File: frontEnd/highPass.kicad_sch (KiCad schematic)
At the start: 15 parts, among them U101 BGS12P2L6E6327XTSA1, U102 BGS12P2L6E6327XTSA1

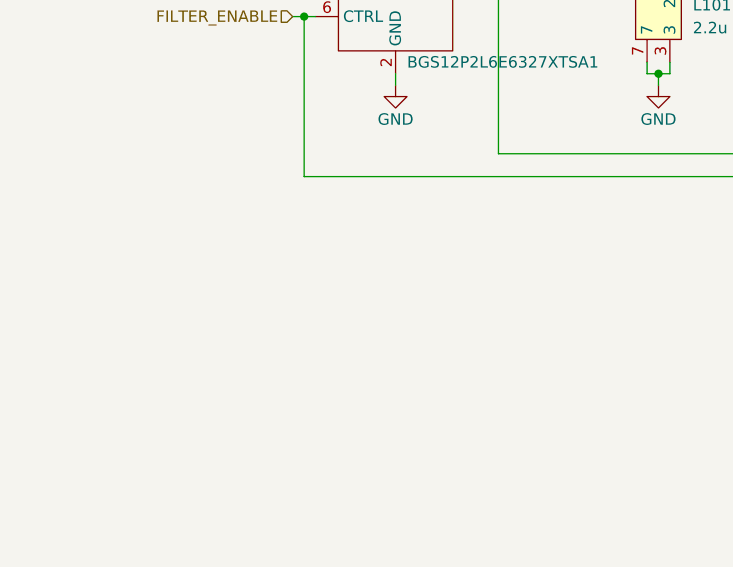
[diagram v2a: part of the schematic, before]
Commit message: add leds for each filter block
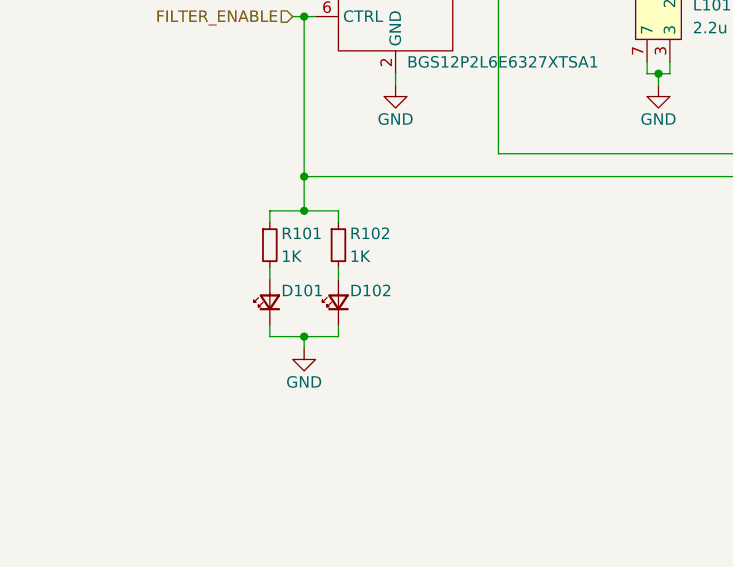
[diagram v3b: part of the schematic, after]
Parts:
- added D101, D102: LED_Small, LED_SMD:LED_0805_2012Metric, symbol Device:LED_Small
- added R101, R102: 1K, Resistor_SMD:R_0805_2012Metric, symbol Device:R_Small
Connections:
- net FILTER_ENABLE: now also R101.1, R102.1
- net GND: now also D101.1 (K), D102.1 (K)
- new net: D102.2 (A), R102.2
- new net: D101.2 (A), R101.2
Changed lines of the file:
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@@
 (kicad_sch (version 20211123) (generator eeschema)
   (paper "A4")
+  (junction (at 66.04 110.49) (diameter 0) (color 0 0 0 0)
+  )
   (junction (at 123.19 95.25) (diameter 0) (color 0 0 0 0)
   )
@@
   (junction (at 158.75 95.25) (diameter 0) (color 0 0 0 0)
   )
+  (junction (at 66.04 124.46) (diameter 0) (color 0 0 0 0)
+  )
   (junction (at 106.68 81.28) (diameter 0) (color 0 0 0 0)
   )
@@
   (junction (at 194.31 95.25) (diameter 0) (color 0 0 0 0)
   )
+  (junction (at 66.04 106.68) (diameter 0) (color 0 0 0 0)
+  )
   (junction (at 142.24 81.28) (diameter 0) (color 0 0 0 0)
   )
@@
     (stroke (width 0) (type default) (color 0 0 0 0))
   )
+  (wire (pts (xy 62.23 124.46) (xy 66.04 124.46))
+    (stroke (width 0) (type default) (color 0 0 0 0))
+  )
   (wire (pts (xy 38.1 175.26) (xy 41.91 175.26))
     (stroke (width 0) (type default) (color 0 0 0 0))
@@
     (stroke (width 0) (type default) (color 0 0 0 0))
   )
+  (wire (pts (xy 69.85 116.84) (xy 69.85 118.11))
+    (stroke (width 0) (type default) (color 0 0 0 0))
+  )
   (wire (pts (xy 45.72 173.99) (xy 45.72 175.26))
     (stroke (width 0) (type default) (color 0 0 0 0))
@@
     (stroke (width 0) (type default) (color 0 0 0 0))
   )
+  (wire (pts (xy 62.23 116.84) (xy 62.23 118.11))
+    (stroke (width 0) (type default) (color 0 0 0 0))
+  )
   (wire (pts (xy 76.2 95.25) (xy 76.2 96.52))
     (stroke (width 0) (type default) (color 0 0 0 0))
@@
     (stroke (width 0) (type default) (color 0 0 0 0))
   )
+  (wire (pts (xy 66.04 124.46) (xy 69.85 124.46))
+    (stroke (width 0) (type default) (color 0 0 0 0))
+  )
   (wire (pts (xy 38.1 167.64) (xy 41.91 167.64))
     (stroke (width 0) (type default) (color 0 0 0 0))
@@
     (stroke (width 0) (type default) (color 0 0 0 0))
   )
+  (wire (pts (xy 66.04 110.49) (xy 69.85 110.49))
+    (stroke (width 0) (type default) (color 0 0 0 0))
+  )
   (wire (pts (xy 66.04 88.9) (xy 66.04 106.68))
     (stroke (width 0) (type default) (color 0 0 0 0))
@@
     (stroke (width 0) (type default) (color 0 0 0 0))
   )
+  (wire (pts (xy 66.04 106.68) (xy 66.04 110.49))
+    (stroke (width 0) (type default) (color 0 0 0 0))
+  )
   (wire (pts (xy 193.04 95.25) (xy 194.31 95.25))
     (stroke (width 0) (type default) (color 0 0 0 0))
@@
     (stroke (width 0) (type default) (color 0 0 0 0))
   )
+  (wire (pts (xy 62.23 123.19) (xy 62.23 124.46))
+    (stroke (width 0) (type default) (color 0 0 0 0))
+  )
+  (wire (pts (xy 69.85 123.19) (xy 69.85 124.46))
+    (stroke (width 0) (type default) (color 0 0 0 0))
+  )
   (wire (pts (xy 38.1 173.99) (xy 38.1 175.26))
     (stroke (width 0) (type default) (color 0 0 0 0))
@@
     (stroke (width 0) (type default) (color 0 0 0 0))
   )
+  (wire (pts (xy 66.04 124.46) (xy 66.04 125.73))
+    (stroke (width 0) (type default) (color 0 0 0 0))
+  )
   (wire (pts (xy 177.8 93.98) (xy 177.8 95.25))
     (stroke (width 0) (type default) (color 0 0 0 0))
@@
     (stroke (width 0) (type default) (color 0 0 0 0))
   )
+  (wire (pts (xy 62.23 111.76) (xy 62.23 110.49))
+    (stroke (width 0) (type default) (color 0 0 0 0))
+  )
   (wire (pts (xy 41.91 166.37) (xy 41.91 167.64))
     (stroke (width 0) (type default) (color 0 0 0 0))
@@
     (stroke (width 0) (type default) (color 0 0 0 0))
   )
+  (wire (pts (xy 69.85 110.49) (xy 69.85 111.76))
+    (stroke (width 0) (type default) (color 0 0 0 0))
+  )
   (wire (pts (xy 228.6 88.9) (xy 226.06 88.9))
     (stroke (width 0) (type default) (color 0 0 0 0))
@@
   )
   (wire (pts (xy 121.92 93.98) (xy 121.92 95.25))
+    (stroke (width 0) (type default) (color 0 0 0 0))
+  )
+  (wire (pts (xy 62.23 110.49) (xy 66.04 110.49))
     (stroke (width 0) (type default) (color 0 0 0 0))
   )
@@
   (hierarchical_label "FILTER_ENABLE" (shape input) (at 64.77 88.9 180)
     (effects (font (size 1.27 1.27)) (justify right))
+  )
+  (symbol (lib_id "Device:LED_Small") (at 69.85 120.65 90) (unit 1)
+    (in_bom yes) (on_board yes)
+    (property "Reference" "D102" (id 0) (at 71.12 119.38 90)
+      (effects (font (size 1.27 1.27)) (justify right))
+    )
+    (property "Value" "LED_Small" (id 1) (at 72.39 121.8564 90)
+      (effects (font (size 1.27 1.27)) (justify right) hide)
+    )
+    (property "Footprint" "LED_SMD:LED_0805_2012Metric" (id 2) (at 69.85 120.65 90)
+      (effects (font (size 1.27 1.27)) hide)
+    )
+    (property "Datasheet" "~" (id 3) (at 69.85 120.65 90)
+      (effects (font (size 1.27 1.27)) hide)
+    )
+    (pin "1")
+    (pin "2")
   )
   (symbol (lib_id "Device:C_Small") (at 45.72 171.45 180) (unit 1)
@@
     (pin "7")
   )
+  (symbol (lib_id "Device:R_Small") (at 62.23 114.3 0) (unit 1)
+    (in_bom yes) (on_board yes)
+    (property "Reference" "R101" (id 0) (at 63.5 113.03 0)
+      (effects (font (size 1.27 1.27)) (justify left))
+    )
+    (property "Value" "1K" (id 1) (at 63.5 115.57 0)
+      (effects (font (size 1.27 1.27)) (justify left))
+    )
+    (property "Footprint" "Resistor_SMD:R_0805_2012Metric" (id 2) (at 62.23 114.3 0)
+      (effects (font (size 1.27 1.27)) hide)
+    )
+    (property "Datasheet" "~" (id 3) (at 62.23 114.3 0)
+      (effects (font (size 1.27 1.27)) hide)
+    )
+    (pin "1")
+    (pin "2")
+  )
   (symbol (lib_id "Device:C_Small") (at 38.1 171.45 180) (unit 1)
     (in_bom yes) (on_board yes)
@@
     (pin "2")
   )
+  (symbol (lib_id "Device:LED_Small") (at 62.23 120.65 90) (unit 1)
+    (in_bom yes) (on_board yes)
+    (property "Reference" "D101" (id 0) (at 63.5 119.38 90)
+      (effects (font (size 1.27 1.27)) (justify right))
+    )
+    (property "Value" "LED_Small" (id 1) (at 64.77 121.8564 90)
+      (effects (font (size 1.27 1.27)) (justify right) hide)
+    )
+    (property "Footprint" "LED_SMD:LED_0805_2012Metric" (id 2) (at 62.23 120.65 90)
+      (effects (font (size 1.27 1.27)) hide)
+    )
+    (property "Datasheet" "~" (id 3) (at 62.23 120.65 90)
+      (effects (font (size 1.27 1.27)) hide)
+    )
+    (pin "1")
+    (pin "2")
+  )
   (symbol (lib_id "Device:C_Small") (at 133.35 81.28 90) (unit 1)
     (in_bom yes) (on_board yes)
@@
     (pin "7")
   )
+  (symbol (lib_id "power:GND") (at 66.04 125.73 0) (unit 1)
+    (in_bom yes) (on_board yes)
+    (property "Reference" "#PWR?" (id 0) (at 66.04 132.08 0)
+      (effects (font (size 1.27 1.27)) hide)
+    )
+    (property "Value" "GND" (id 1) (at 66.04 129.54 0))
+    (property "Footprint" "" (id 2) (at 66.04 125.73 0)
+      (effects (font (size 1.27 1.27)) hide)
+    )
+    (property "Datasheet" "" (id 3) (at 66.04 125.73 0)
+      (effects (font (size 1.27 1.27)) hide)
+    )
+    (pin "1")
+  )
   (symbol (lib_id "Device:C_Small") (at 186.69 81.28 90) (unit 1)
     (in_bom yes) (on_board yes)
@@
     (pin "1")
   )
+  (symbol (lib_id "Device:R_Small") (at 69.85 114.3 0) (unit 1)
+    (in_bom yes) (on_board yes)
+    (property "Reference" "R102" (id 0) (at 71.12 113.03 0)
+      (effects (font (size 1.27 1.27)) (justify left))
+    )
+    (property "Value" "1K" (id 1) (at 71.12 115.57 0)
+      (effects (font (size 1.27 1.27)) (justify left))
+    )
+    (property "Footprint" "Resistor_SMD:R_0805_2012Metric" (id 2) (at 69.85 114.3 0)
+      (effects (font (size 1.27 1.27)) hide)
+    )
+    (property "Datasheet" "~" (id 3) (at 69.85 114.3 0)
+      (effects (font (size 1.27 1.27)) hide)
+    )
+    (pin "1")
+    (pin "2")
+  )
   (symbol (lib_id "power:GND") (at 76.2 96.52 0) (unit 1)

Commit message: assign footprints, part designators
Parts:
- U101, U102: footprint (none) -> frontEnd:BGS12P2L6E6327XTSA1
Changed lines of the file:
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@@
   (symbol (lib_id "power:GND") (at 105.41 96.52 0) (unit 1)
     (in_bom yes) (on_board yes)
-    (property "Reference" "#PWR?" (id 0) (at 105.41 102.87 0)
+    (property "Reference" "#PWR0124" (id 0) (at 105.41 102.87 0)
       (effects (font (size 1.27 1.27)) hide)
     )
@@
   (symbol (lib_id "power:+3V3") (at 41.91 166.37 0) (unit 1)
     (in_bom yes) (on_board yes)
-    (property "Reference" "#PWR?" (id 0) (at 41.91 170.18 0)
+    (property "Reference" "#PWR0129" (id 0) (at 41.91 170.18 0)
       (effects (font (size 1.27 1.27)) hide)
     )
@@
   (symbol (lib_id "power:GND") (at 217.17 96.52 0) (unit 1)
     (in_bom yes) (on_board yes)
-    (property "Reference" "#PWR?" (id 0) (at 217.17 102.87 0)
+    (property "Reference" "#PWR0122" (id 0) (at 217.17 102.87 0)
       (effects (font (size 1.27 1.27)) hide)
     )
@@
       (effects (font (size 1.27 1.27)) (justify left))
     )
-    (property "Footprint" "" (id 2) (at 69.85 83.82 0)
+    (property "Footprint" "frontEnd:BGS12P2L6E6327XTSA1" (id 2) (at 69.85 83.82 0)
       (effects (font (size 1.27 1.27)) hide)
     )
@@
   (symbol (lib_id "power:GND") (at 176.53 96.52 0) (unit 1)
     (in_bom yes) (on_board yes)
-    (property "Reference" "#PWR?" (id 0) (at 176.53 102.87 0)
+    (property "Reference" "#PWR0119" (id 0) (at 176.53 102.87 0)
       (effects (font (size 1.27 1.27)) hide)
     )
@@
   (symbol (lib_id "power:GND") (at 41.91 176.53 0) (unit 1)
     (in_bom yes) (on_board yes)
-    (property "Reference" "#PWR?" (id 0) (at 41.91 182.88 0)
+    (property "Reference" "#PWR0128" (id 0) (at 41.91 182.88 0)
       (effects (font (size 1.27 1.27)) hide)
     )
@@
   (symbol (lib_id "power:GND") (at 158.75 96.52 0) (unit 1)
     (in_bom yes) (on_board yes)
-    (property "Reference" "#PWR?" (id 0) (at 158.75 102.87 0)
+    (property "Reference" "#PWR0117" (id 0) (at 158.75 102.87 0)
       (effects (font (size 1.27 1.27)) hide)
     )
@@
   (symbol (lib_id "power:GND") (at 123.19 96.52 0) (unit 1)
     (in_bom yes) (on_board yes)
-    (property "Reference" "#PWR?" (id 0) (at 123.19 102.87 0)
+    (property "Reference" "#PWR0120" (id 0) (at 123.19 102.87 0)
       (effects (font (size 1.27 1.27)) hide)
     )
@@
   (symbol (lib_id "power:GND") (at 66.04 125.73 0) (unit 1)
     (in_bom yes) (on_board yes)
-    (property "Reference" "#PWR?" (id 0) (at 66.04 132.08 0)
+    (property "Reference" "#PWR0127" (id 0) (at 66.04 132.08 0)
       (effects (font (size 1.27 1.27)) hide)
     )
@@
   (symbol (lib_id "power:+3V3") (at 217.17 74.93 0) (unit 1)
     (in_bom yes) (on_board yes)
-    (property "Reference" "#PWR?" (id 0) (at 217.17 78.74 0)
+    (property "Reference" "#PWR0121" (id 0) (at 217.17 78.74 0)
       (effects (font (size 1.27 1.27)) hide)
     )
@@
   (symbol (lib_id "power:GND") (at 76.2 96.52 0) (unit 1)
     (in_bom yes) (on_board yes)
-    (property "Reference" "#PWR?" (id 0) (at 76.2 102.87 0)
+    (property "Reference" "#PWR0125" (id 0) (at 76.2 102.87 0)
       (effects (font (size 1.27 1.27)) hide)
     )
@@
   (symbol (lib_id "power:GND") (at 140.97 96.52 0) (unit 1)
     (in_bom yes) (on_board yes)
-    (property "Reference" "#PWR?" (id 0) (at 140.97 102.87 0)
+    (property "Reference" "#PWR0118" (id 0) (at 140.97 102.87 0)
       (effects (font (size 1.27 1.27)) hide)
     )
@@
       (effects (font (size 1.27 1.27)) (justify left))
     )
-    (property "Footprint" "" (id 2) (at 223.52 83.82 0)
+    (property "Footprint" "frontEnd:BGS12P2L6E6327XTSA1" (id 2) (at 223.52 83.82 0)
       (effects (font (size 1.27 1.27)) hide)
     )
@@
   (symbol (lib_id "power:+3V3") (at 76.2 74.93 0) (unit 1)
     (in_bom yes) (on_board yes)
-    (property "Reference" "#PWR?" (id 0) (at 76.2 78.74 0)
+    (property "Reference" "#PWR0126" (id 0) (at 76.2 78.74 0)
       (effects (font (size 1.27 1.27)) hide)
     )
@@
   (symbol (lib_id "power:GND") (at 194.31 96.52 0) (unit 1)
     (in_bom yes) (on_board yes)
-    (property "Reference" "#PWR?" (id 0) (at 194.31 102.87 0)
-      (effects (font (size 1.27 1.27)) hide)
-    )
+    (property "Reference" "#PWR0123" (id 0) (at 194.31 102.87 0)
+      (effects (font (size 1.27 1.27)) hide)
+    )

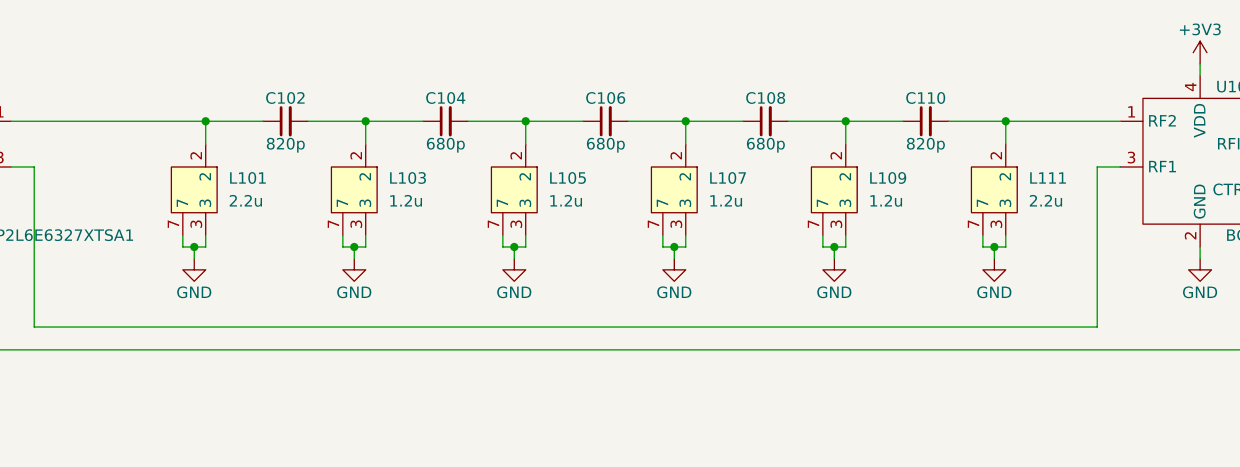
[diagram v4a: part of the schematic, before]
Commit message: convert all embeded filter to plug-in modules, start pcb layout
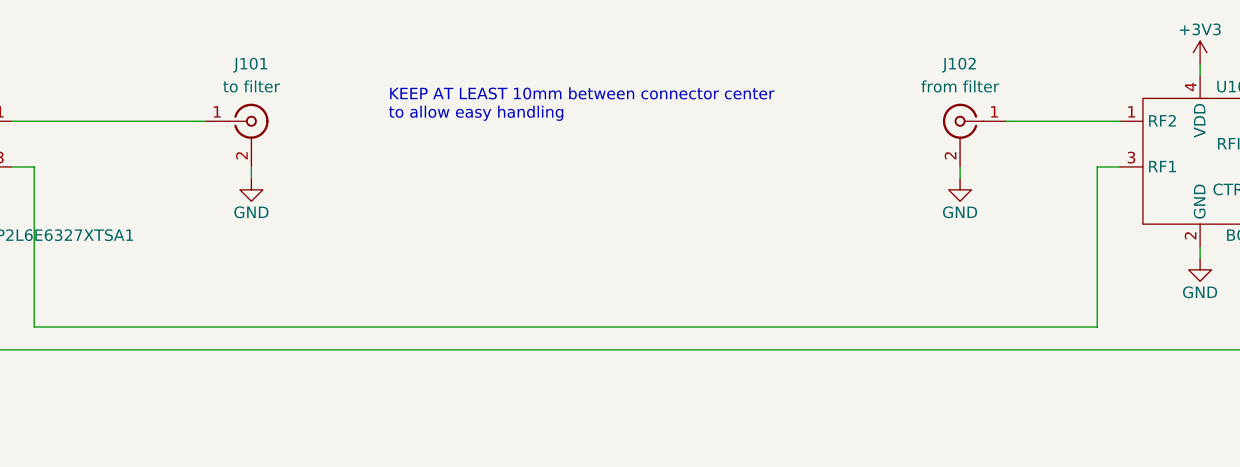
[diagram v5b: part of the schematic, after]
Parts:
- removed C102, C110: 820p, Capacitor_SMD:C_0805_2012Metric, symbol Device:C_Small
- removed C104, C106, C108: 680p, Capacitor_SMD:C_0805_2012Metric, symbol Device:C_Small
- removed L101, L111: 2.2u, frontEnd:TOKO_10K, symbol frontEnd:TOKO_10K
- removed L103, L105, L107, L109: 1.2u, frontEnd:TOKO_10K, symbol frontEnd:TOKO_10K
- added J101: to filter, frontEnd:SMA_FEM_TH_VERTICAL, symbol Connector:Conn_Coaxial
- added J102: from filter, frontEnd:SMA_FEM_TH_VERTICAL, symbol Connector:Conn_Coaxial
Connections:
- net GND: now also J101.2 (Ext), J102.2 (Ext)
- net at U101.1 (RF2): now also J101.1 (In)
- net at U102.1 (RF2): now also J102.1 (In)
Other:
- note added: "KEEP AT LEAST 10mm between connector center to allow easy handling"
